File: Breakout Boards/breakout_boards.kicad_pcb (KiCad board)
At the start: 4 copper layers, 72.5 x 61.5 mm, 54 parts, among them J10 Conn_01x04_Pin, J11 Conn_01x04_Pin, J12 Conn_01x04_Pin, J13 Conn_01x04_Pin, J14 Conn_01x04_Pin, J15 Conn_01x04_Pin, J16 Conn_01x04_Pin, J17 Conn_01x04_Pin, J18 Conn_01x04_Pin, J19 Conn_01x04_Pin, J9 Conn_01x04_Pin, Q5 NPN BJT

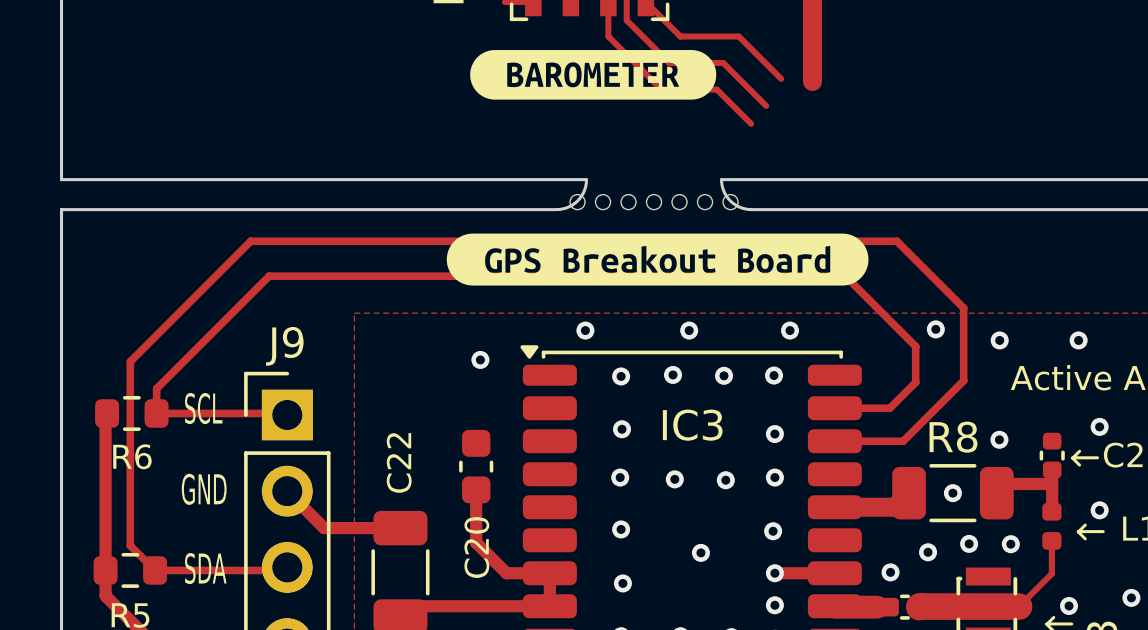
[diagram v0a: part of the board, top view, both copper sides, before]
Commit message: Minor changes
Minor changes to the srad fab layer(added dimensions) and two traces in the GPS breakout board.
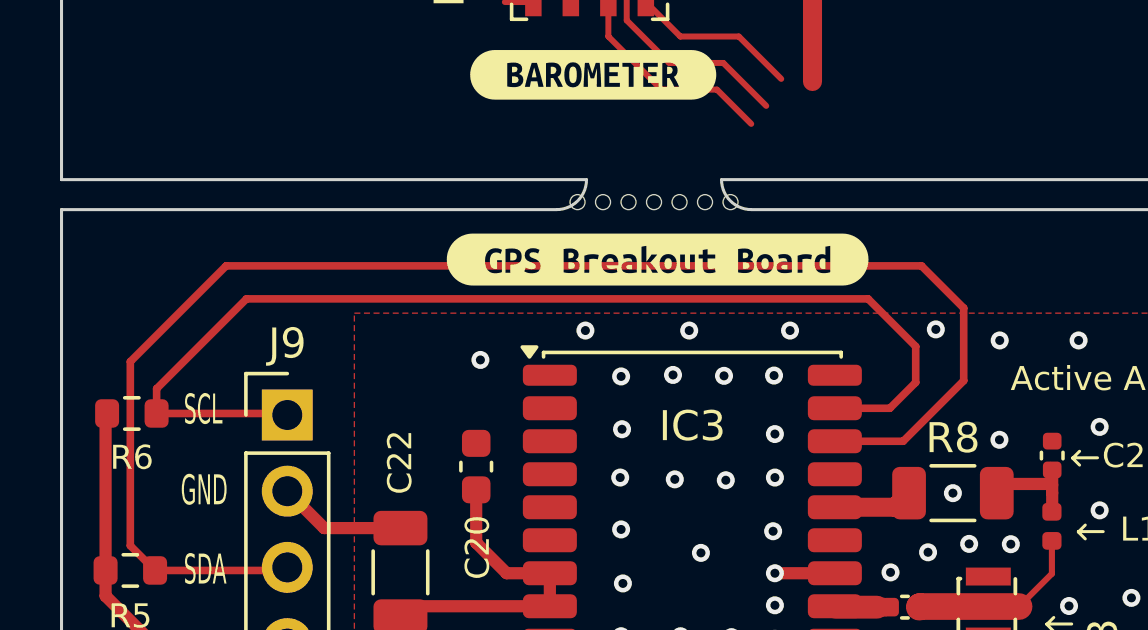
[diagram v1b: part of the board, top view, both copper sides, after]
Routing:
- net GPS_SDA: track 49.7 -> 49.0 mm
- net GPS_SCL: track 37.3 -> 36.7 mm
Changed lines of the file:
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@@
 	)
 	(segment
-		(start 77.573006 95.981809)
-		(end 77.573006 98.403397)
+		(start 49.7936 103.902603)
+		(end 49.7936 97.768003)
 		(width 0.254)
 		(layer "F.Cu")
@@
 	)
 	(segment
+		(start 75.5556 100.420803)
+		(end 73.278002 100.420803)
+		(width 0.254)
+		(layer "F.Cu")
+		(net "GPS_SDA")
+	)
+	(segment
+		(start 77.573006 98.403397)
+		(end 75.5556 100.420803)
+		(width 0.254)
+		(layer "F.Cu")
+		(net "GPS_SDA")
+	)
+	(segment
 		(start 50.6186 104.727603)
 		(end 49.7936 103.902603)
@@
 	)
 	(segment
-		(start 75.5556 100.420803)
-		(end 73.278002 100.420803)
+		(start 77.573006 95.981809)
+		(end 77.573006 98.403397)
 		(width 0.254)
 		(layer "F.Cu")
@@
 	)
 	(segment
-		(start 75.346 93.754803)
+		(start 76.166197 94.575)
 		(end 77.573006 95.981809)
 		(width 0.254)
@@
 	)
 	(segment
-		(start 49.7936 97.768003)
-		(end 53.8068 93.754803)
+		(start 52.986603 94.575)
+		(end 76.166197 94.575)
 		(width 0.254)
 		(layer "F.Cu")
@@
 	)
 	(segment
-		(start 77.573006 98.403397)
-		(end 75.5556 100.420803)
+		(start 49.7936 97.768003)
+		(end 52.986603 94.575)
 		(width 0.254)
 		(layer "F.Cu")
@@
 	)
 	(segment
-		(start 53.8068 93.754803)
-		(end 75.346 93.754803)
-		(width 0.254)
-		(layer "F.Cu")
-		(net "GPS_SDA")
-	)
-	(segment
-		(start 49.7936 103.902603)
-		(end 49.7936 97.768003)
-		(width 0.254)
-		(layer "F.Cu")
-		(net "GPS_SDA")
-	)
-	(segment
-		(start 73.631206 94.919003)
-		(end 75.973006 97.260803)
+		(start 50.6694 99.495203)
+		(end 54.9752 99.495203)
 		(width 0.254)
 		(layer "F.Cu")
@@
 	)
 	(segment
-		(start 50.6694 99.495203)
-		(end 54.9752 99.495203)
+		(start 75.973006 97.260803)
+		(end 75.973006 98.460803)
 		(width 0.254)
 		(layer "F.Cu")
@@
 	)
 	(segment
-		(start 75.973006 97.260803)
-		(end 75.973006 98.460803)
+		(start 75.973006 98.460803)
+		(end 75.113006 99.320803)
 		(width 0.254)
 		(layer "F.Cu")
@@
 	(segment
 		(start 50.6694 98.670203)
-		(end 54.4206 94.919003)
+		(end 53.664603 95.675)
 		(width 0.254)
 		(layer "F.Cu")
@@
 	)
 	(segment
-		(start 50.6694 99.495203)
-		(end 50.6694 98.670203)
-		(width 0.254)
-		(layer "F.Cu")
-		(net "GPS_SCL")
-	)
-	(segment
-		(start 75.973006 98.460803)
-		(end 75.113006 99.320803)
+		(start 53.664603 95.675)
+		(end 74.387203 95.675)
 		(width 0.254)
 		(layer "F.Cu")
@@
 	)
 	(segment
-		(start 54.4206 94.919003)
-		(end 73.631206 94.919003)
+		(start 74.387203 95.675)
+		(end 75.973006 97.260803)
 		(width 0.254)
 		(layer "F.Cu")
+		(net "GPS_SCL")
+	)
+	(segment
+		(start 50.6694 99.495203)
+		(end 50.6694 98.670203)
+		(width 0.254)
+		(layer "F.Cu")
